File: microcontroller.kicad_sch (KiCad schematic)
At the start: 13 parts, among them IC1 ATMEGA2560-16AU, J1 ICSP, Y1 16Mghz

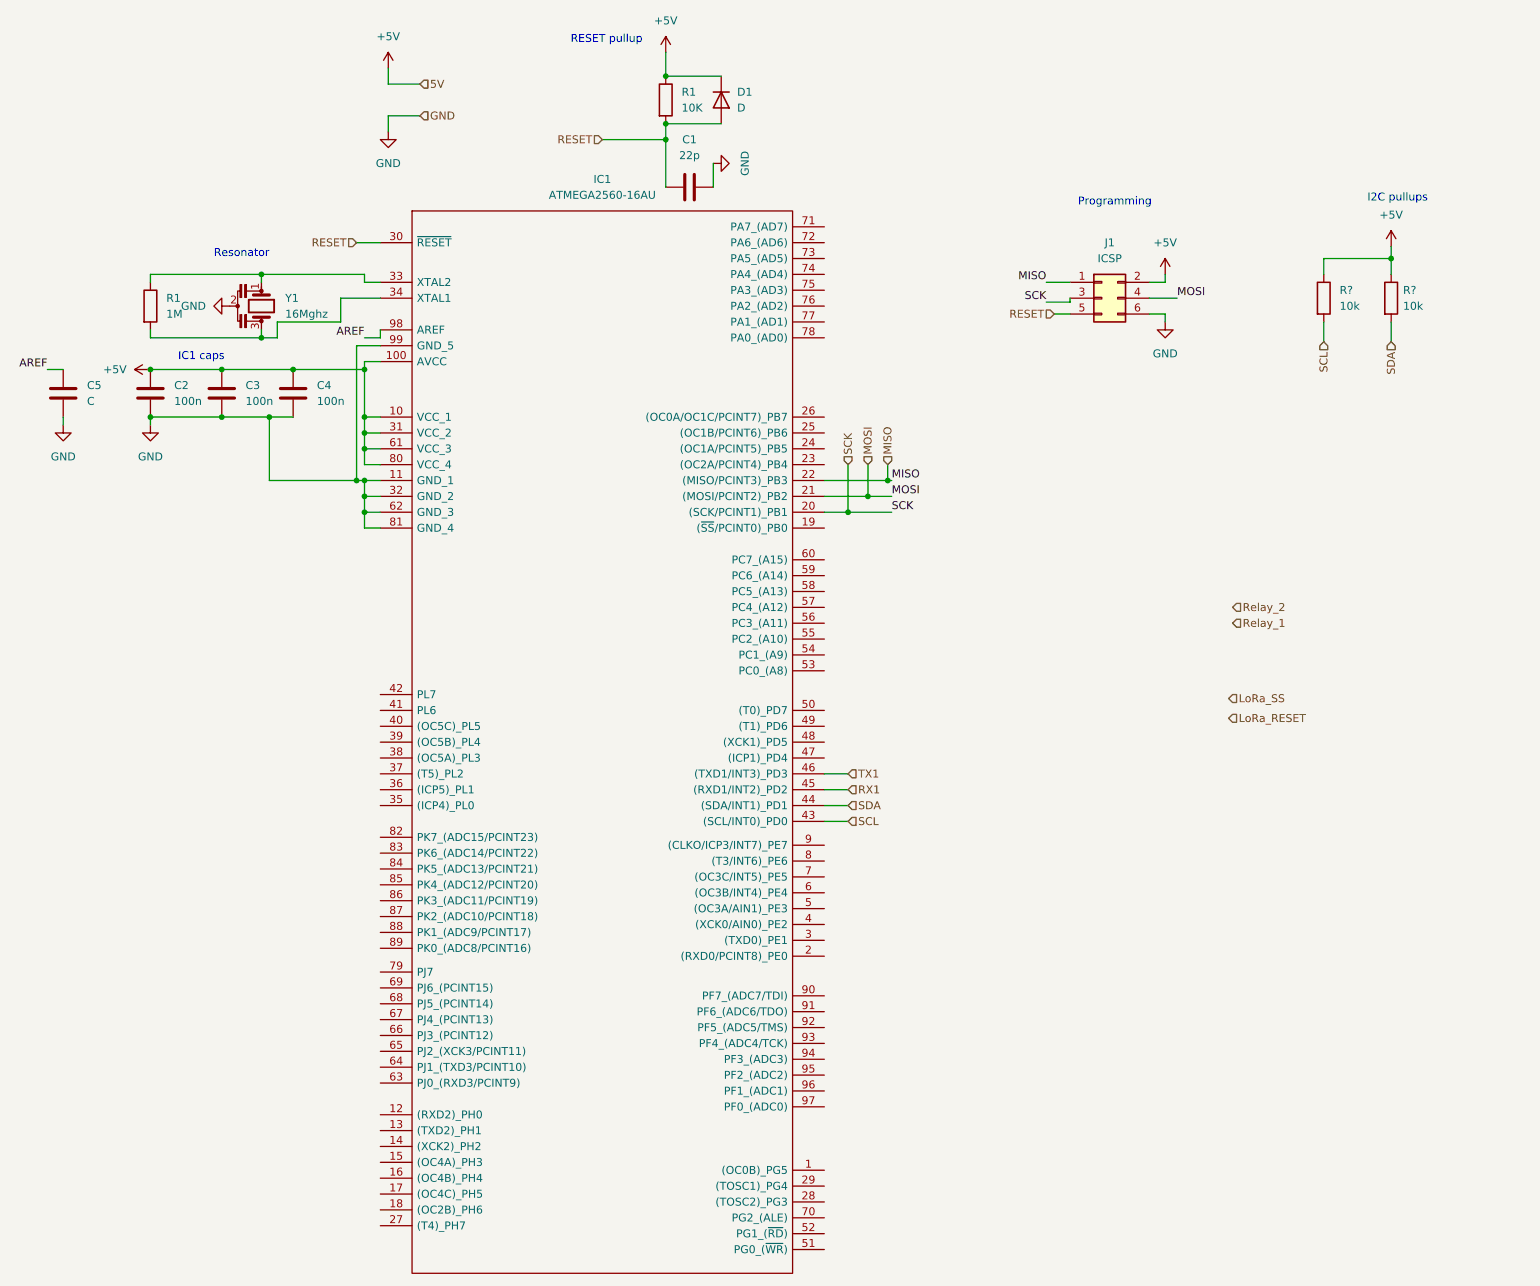
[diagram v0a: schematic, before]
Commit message: atmega2560 at 3v3 now. almost done with  SD card
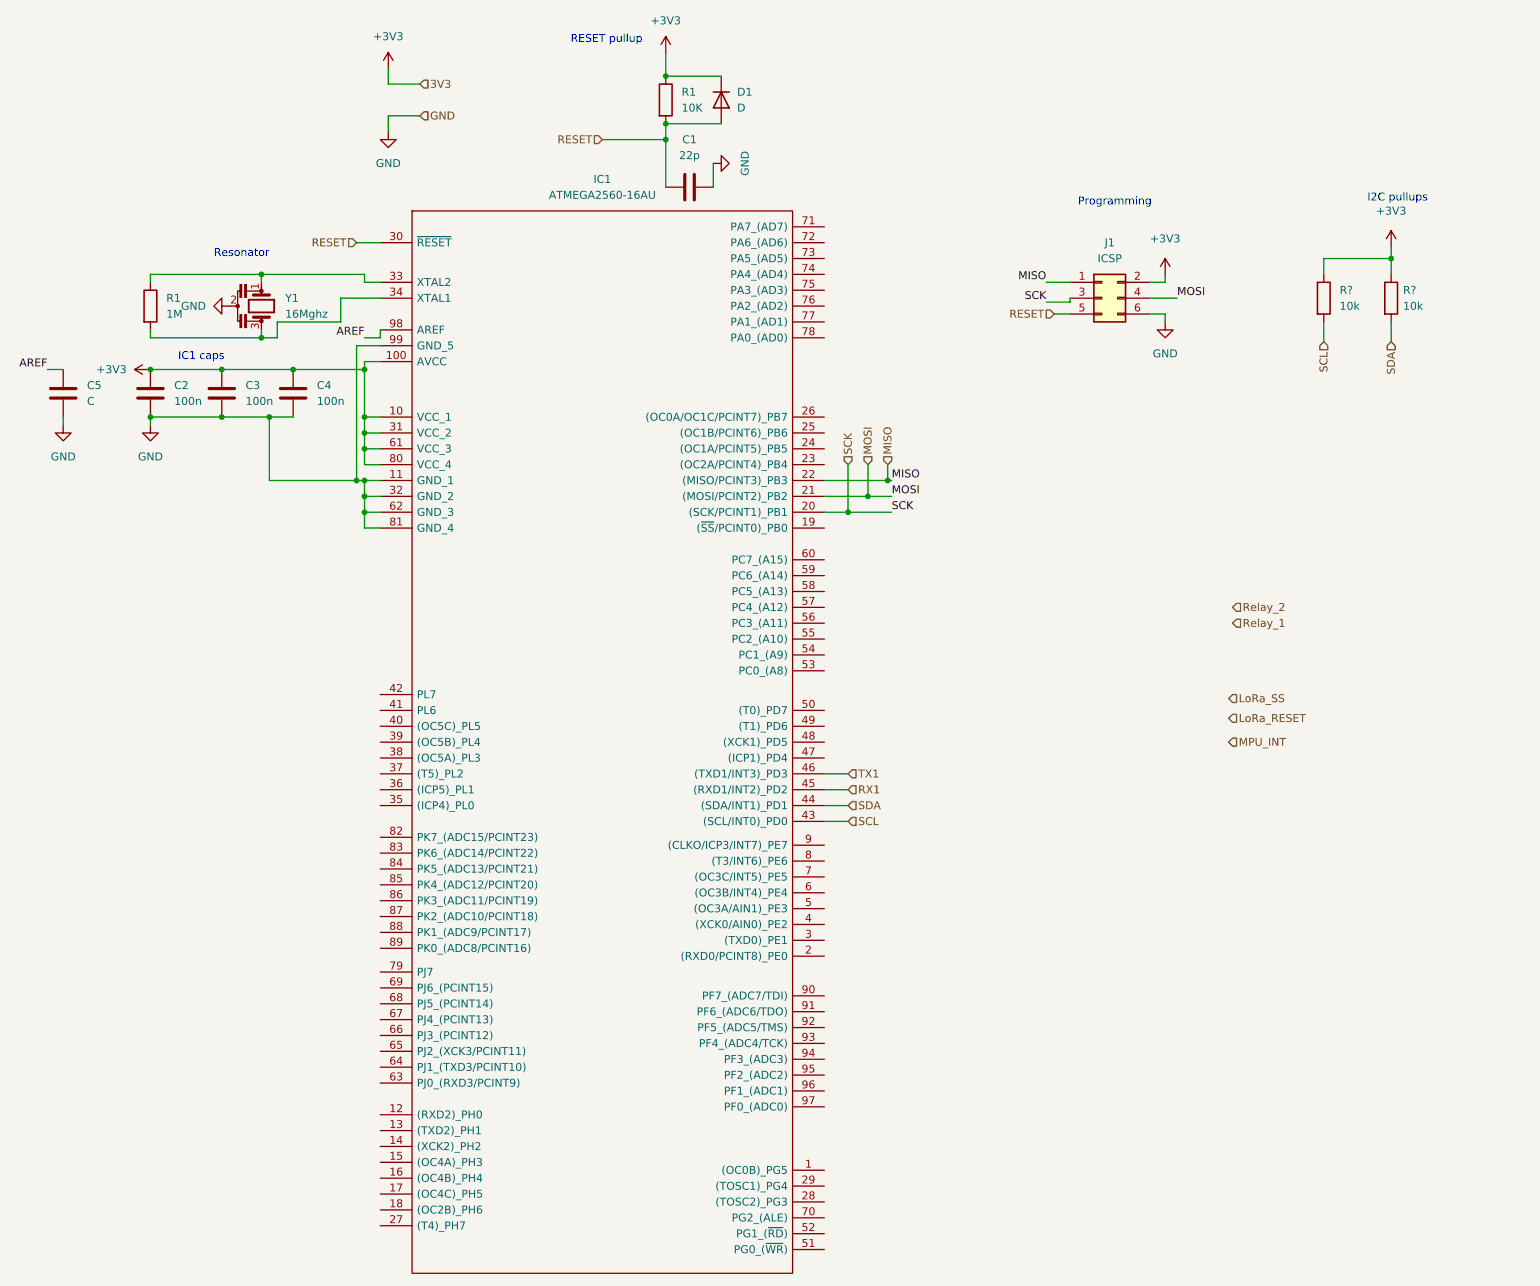
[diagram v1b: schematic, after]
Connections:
- net +5V renamed +3V3
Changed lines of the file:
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@@
   (junction (at 116.84 22.86) (diameter 0) (color 0 0 0 0)
   )
+  (junction (at 34.29 69.85) (diameter 0) (color 0 0 0 0)
+  )
   (junction (at 152.4 87.63) (diameter 0) (color 0 0 0 0)
   )
@@
   )
   (junction (at 68.58 90.17) (diameter 0) (color 0 0 0 0)
-  )
-  (junction (at 34.29 69.85) (diameter 0) (color 0 0 0 0)
   )
   (junction (at 45.72 77.47) (diameter 0) (color 0 0 0 0)
@@
     (effects (font (size 1.27 1.27)) (justify left))
   )
-  (hierarchical_label "5V" (shape input) (at 77.47 24.13 0)
+  (hierarchical_label "3V3" (shape input) (at 77.47 24.13 0)
+    (effects (font (size 1.27 1.27)) (justify left))
+  )
+  (hierarchical_label "MPU_INT" (shape input) (at 207.01 129.54 0)
     (effects (font (size 1.27 1.27)) (justify left))
   )
@@
   (hierarchical_label "SCL" (shape input) (at 222.25 65.405 270)
     (effects (font (size 1.27 1.27)) (justify right))
+  )
+  (symbol (lib_id "power:+3V3") (at 233.045 50.165 0) (unit 1)
+    (in_bom yes) (on_board yes) (fields_autoplaced)
+    (property "Reference" "#PWR?" (id 0) (at 233.045 53.975 0)
+      (effects (font (size 1.27 1.27)) hide)
+    )
+    (property "Value" "+3V3" (id 1) (at 233.045 44.45 0))
+    (property "Footprint" "" (id 2) (at 233.045 50.165 0)
+      (effects (font (size 1.27 1.27)) hide)
+    )
+    (property "Datasheet" "" (id 3) (at 233.045 50.165 0)
+      (effects (font (size 1.27 1.27)) hide)
+    )
+    (pin "1")
   )
   (symbol (lib_id "power:GND") (at 72.39 31.75 0) (unit 1)
@@
     (pin "2")
   )
-  (symbol (lib_id "power:+5V") (at 196.85 54.61 0) (unit 1)
-    (in_bom yes) (on_board yes) (fields_autoplaced)
-    (property "Reference" "#PWR0112" (id 0) (at 196.85 58.42 0)
-      (effects (font (size 1.27 1.27)) hide)
-    )
-    (property "Value" "+5V" (id 1) (at 196.85 49.53 0))
-    (property "Footprint" "" (id 2) (at 196.85 54.61 0)
-      (effects (font (size 1.27 1.27)) hide)
-    )
-    (property "Datasheet" "" (id 3) (at 196.85 54.61 0)
-      (effects (font (size 1.27 1.27)) hide)
-    )
-    (pin "1")
-  )
   (symbol (lib_id "power:GND") (at 124.46 36.83 90) (unit 1)
     (in_bom yes) (on_board yes) (fields_autoplaced)
@@
     (pin "1")
   )
+  (symbol (lib_id "power:+3V3") (at 72.39 21.59 0) (unit 1)
+    (in_bom yes) (on_board yes) (fields_autoplaced)
+    (property "Reference" "#PWR?" (id 0) (at 72.39 25.4 0)
+      (effects (font (size 1.27 1.27)) hide)
+    )
+    (property "Value" "+3V3" (id 1) (at 72.39 16.51 0))
+    (property "Footprint" "" (id 2) (at 72.39 21.59 0)
+      (effects (font (size 1.27 1.27)) hide)
+    )
+    (property "Datasheet" "" (id 3) (at 72.39 21.59 0)
+      (effects (font (size 1.27 1.27)) hide)
+    )
+    (pin "1")
+  )
   (symbol (lib_id "power:GND") (at 20.32 78.74 0) (unit 1)
     (in_bom yes) (on_board yes) (fields_autoplaced)
@@
     (pin "1")
   )
+  (symbol (lib_id "power:+3V3") (at 116.84 19.05 0) (unit 1)
+    (in_bom yes) (on_board yes) (fields_autoplaced)
+    (property "Reference" "#PWR?" (id 0) (at 116.84 22.86 0)
+      (effects (font (size 1.27 1.27)) hide)
+    )
+    (property "Value" "+3V3" (id 1) (at 116.84 13.97 0))
+    (property "Footprint" "" (id 2) (at 116.84 19.05 0)
+      (effects (font (size 1.27 1.27)) hide)
+    )
+    (property "Datasheet" "" (id 3) (at 116.84 19.05 0)
+      (effects (font (size 1.27 1.27)) hide)
+    )
+    (pin "1")
+  )
   (symbol (lib_id "power:GND") (at 46.99 59.69 270) (mirror x) (unit 1)
     (in_bom yes) (on_board yes) (fields_autoplaced)
@@
     (pin "1")
     (pin "2")
-  )
-  (symbol (lib_id "power:+5V") (at 34.29 69.85 90) (unit 1)
-    (in_bom yes) (on_board yes) (fields_autoplaced)
-    (property "Reference" "#PWR0108" (id 0) (at 38.1 69.85 0)
-      (effects (font (size 1.27 1.27)) hide)
-    )
-    (property "Value" "+5V" (id 1) (at 30.48 69.8499 90)
-      (effects (font (size 1.27 1.27)) (justify left))
-    )
-    (property "Footprint" "" (id 2) (at 34.29 69.85 0)
-      (effects (font (size 1.27 1.27)) hide)
-    )
-    (property "Datasheet" "" (id 3) (at 34.29 69.85 0)
-      (effects (font (size 1.27 1.27)) hide)
-    )
-    (pin "1")
   )
   (symbol (lib_id "Device:C") (at 45.72 73.66 0) (unit 1)
@@
     (pin "3")
   )
-  (symbol (lib_id "power:+5V") (at 72.39 21.59 0) (unit 1)
-    (in_bom yes) (on_board yes) (fields_autoplaced)
-    (property "Reference" "#PWR0105" (id 0) (at 72.39 25.4 0)
-      (effects (font (size 1.27 1.27)) hide)
-    )
-    (property "Value" "+5V" (id 1) (at 72.39 16.51 0))
-    (property "Footprint" "" (id 2) (at 72.39 21.59 0)
-      (effects (font (size 1.27 1.27)) hide)
-    )
-    (property "Datasheet" "" (id 3) (at 72.39 21.59 0)
-      (effects (font (size 1.27 1.27)) hide)
-    )
-    (pin "1")
-  )
   (symbol (lib_id "Device:R") (at 34.29 59.69 0) (unit 1)
     (in_bom yes) (on_board yes) (fields_autoplaced)
@@
     (pin "1")
     (pin "2")
+  )
+  (symbol (lib_id "power:+3V3") (at 196.85 54.61 0) (unit 1)
+    (in_bom yes) (on_board yes) (fields_autoplaced)
+    (property "Reference" "#PWR?" (id 0) (at 196.85 58.42 0)
+      (effects (font (size 1.27 1.27)) hide)
+    )
+    (property "Value" "+3V3" (id 1) (at 196.85 48.895 0))
+    (property "Footprint" "" (id 2) (at 196.85 54.61 0)
+      (effects (font (size 1.27 1.27)) hide)
+    )
+    (property "Datasheet" "" (id 3) (at 196.85 54.61 0)
+      (effects (font (size 1.27 1.27)) hide)
+    )
+    (pin "1")
   )
   (symbol (lib_id "power:GND") (at 196.85 62.23 0) (unit 1)
@@
     (pin "1")
   )
+  (symbol (lib_id "power:+3V3") (at 34.29 69.85 90) (unit 1)
+    (in_bom yes) (on_board yes) (fields_autoplaced)
+    (property "Reference" "#PWR?" (id 0) (at 38.1 69.85 0)
+      (effects (font (size 1.27 1.27)) hide)
+    )
+    (property "Value" "+3V3" (id 1) (at 30.48 69.8499 90)
+      (effects (font (size 1.27 1.27)) (justify left))
+    )
+    (property "Footprint" "" (id 2) (at 34.29 69.85 0)
+      (effects (font (size 1.27 1.27)) hide)
+    )
+    (property "Datasheet" "" (id 3) (at 34.29 69.85 0)
+      (effects (font (size 1.27 1.27)) hide)
+    )
+    (pin "1")
+  )
   (symbol (lib_id "Device:D") (at 125.73 26.67 270) (unit 1)
     (in_bom yes) (on_board yes) (fields_autoplaced)
@@
     (pin "1")
     (pin "2")
-  )
-  (symbol (lib_id "power:+5V") (at 233.045 50.165 0) (unit 1)
-    (in_bom yes) (on_board yes) (fields_autoplaced)
-    (property "Reference" "#PWR0111" (id 0) (at 233.045 53.975 0)
-      (effects (font (size 1.27 1.27)) hide)
-    )
-    (property "Value" "+5V" (id 1) (at 233.045 45.085 0))
-    (property "Footprint" "" (id 2) (at 233.045 50.165 0)
-      (effects (font (size 1.27 1.27)) hide)
-    )
-    (property "Datasheet" "" (id 3) (at 233.045 50.165 0)
-      (effects (font (size 1.27 1.27)) hide)
-    )
-    (pin "1")
   )
   (symbol (lib_id "Connector_Generic:Conn_02x03_Odd_Even") (at 186.69 58.42 0) (unit 1)
@@
     (pin "6")
   )
-  (symbol (lib_id "power:+5V") (at 116.84 19.05 0) (unit 1)
-    (in_bom yes) (on_board yes) (fields_autoplaced)
-    (property "Reference" "#PWR0103" (id 0) (at 116.84 22.86 0)
-      (effects (font (size 1.27 1.27)) hide)
-    )
-    (property "Value" "+5V" (id 1) (at 116.84 13.97 0))
-    (property "Footprint" "" (id 2) (at 116.84 19.05 0)
-      (effects (font (size 1.27 1.27)) hide)
-    )
-    (property "Datasheet" "" (id 3) (at 116.84 19.05 0)
-      (effects (font (size 1.27 1.27)) hide)
-    )
-    (pin "1")
-  )
 )

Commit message: updating schematic
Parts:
- C2, C3, C4: value 100n -> 0.1u
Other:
- note added: "Not sure how to deal with ignition detection"
- note added: "Place buzzer on PWM capable pin just in case."
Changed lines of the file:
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@@
     (stroke (width 0) (type default) (color 0 0 0 0))
   )
+  (text "Not sure how to deal with ignition detection\n" (at 201.168 88.773 0)
+    (effects (font (size 1.27 1.27)) (justify left bottom))
+  )
   (text "IC1 caps" (at 38.735 68.58 0)
     (effects (font (size 1.27 1.27)) (justify left bottom))
@@
   )
   (text "Programming" (at 182.88 43.815 0)
+    (effects (font (size 1.27 1.27)) (justify left bottom))
+  )
+  (text "Place buzzer on PWM capable pin just in case.\n" (at 193.929 81.788 0)
     (effects (font (size 1.27 1.27)) (justify left bottom))
   )
@@
     (effects (font (size 1.27 1.27)) (justify right bottom))
   )
-  (hierarchical_label "Relay_1" (shape input) (at 207.645 110.49 0)
+  (hierarchical_label "Relay_1" (shape input) (at 208.153 101.219 0)
     (effects (font (size 1.27 1.27)) (justify left))
   )
@@
     (effects (font (size 1.27 1.27)) (justify right))
   )
-  (hierarchical_label "Relay_2" (shape input) (at 207.645 107.95 0)
+  (hierarchical_label "Relay_2" (shape input) (at 208.153 98.679 0)
     (effects (font (size 1.27 1.27)) (justify left))
   )
@@
     (effects (font (size 1.27 1.27)) (justify left))
   )
+  (hierarchical_label "ID2" (shape input) (at 208.153 92.837 0)
+    (effects (font (size 1.27 1.27)) (justify left))
+  )
   (hierarchical_label "TX1" (shape input) (at 146.05 134.62 0)
     (effects (font (size 1.27 1.27)) (justify left))
   )
+  (hierarchical_label "SD_CS" (shape input) (at 207.01 145.796 0)
+    (effects (font (size 1.27 1.27)) (justify left))
+  )
   (hierarchical_label "SCK" (shape input) (at 146.05 85.09 90)
     (effects (font (size 1.27 1.27)) (justify left))
   )
+  (hierarchical_label "Buzzer" (shape input) (at 208.153 84.328 0)
+    (effects (font (size 1.27 1.27)) (justify left))
+  )
   (hierarchical_label "SDA" (shape input) (at 233.045 65.405 270)
     (effects (font (size 1.27 1.27)) (justify right))
   )
-  (hierarchical_label "LoRa_SS" (shape input) (at 207.01 122.555 0)
+  (hierarchical_label "LoRa_CS" (shape input) (at 207.01 122.555 0)
     (effects (font (size 1.27 1.27)) (justify left))
   )
@@
     (effects (font (size 1.27 1.27)) (justify left))
   )
-  (hierarchical_label "MPU_INT" (shape input) (at 207.01 129.54 0)
+  (hierarchical_label "MPU_INT" (shape input) (at 207.01 135.763 0)
+    (effects (font (size 1.27 1.27)) (justify left))
+  )
+  (hierarchical_label "BMP_INT" (shape input) (at 207.01 138.049 0)
     (effects (font (size 1.27 1.27)) (justify left))
   )
@@
   (hierarchical_label "RESET" (shape input) (at 106.68 33.02 180)
     (effects (font (size 1.27 1.27)) (justify right))
+  )
+  (hierarchical_label "ID1" (shape input) (at 208.153 94.996 0)
+    (effects (font (size 1.27 1.27)) (justify left))
   )
   (hierarchical_label "SCL" (shape input) (at 222.25 65.405 270)
@@
       (effects (font (size 1.27 1.27)) (justify left))
     )
-    (property "Value" "100n" (id 1) (at 60.96 74.9299 0)
+    (property "Value" "0.1u" (id 1) (at 60.96 74.9299 0)
       (effects (font (size 1.27 1.27)) (justify left))
     )
@@
       (effects (font (size 1.27 1.27)) (justify left))
     )
-    (property "Value" "100n" (id 1) (at 38.1 74.9299 0)
+    (property "Value" "0.1u" (id 1) (at 38.1 74.9299 0)
       (effects (font (size 1.27 1.27)) (justify left))
     )
@@
       (effects (font (size 1.27 1.27)) (justify left))
     )
-    (property "Value" "100n" (id 1) (at 49.53 74.9299 0)
-      (effects (font (size 1.27 1.27)) (justify left))
-    )
+    (property "Value" "0.1u" (id 1) (at 49.53 74.9299 0)
+      (effects (font (size 1.27 1.27)) (justify left))
+    )
